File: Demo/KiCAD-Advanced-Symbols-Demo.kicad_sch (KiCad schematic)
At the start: 15 parts

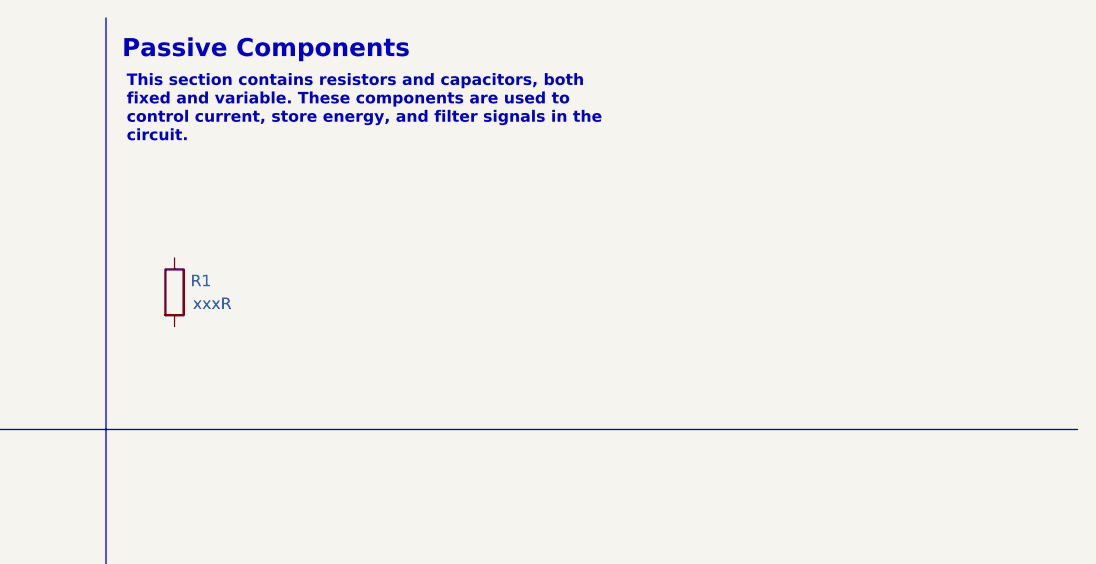
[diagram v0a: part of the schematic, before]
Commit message: Add general and specialized diode symbols, fixed capacitor, and potentiometer
Added new components to library: general diode symbols (Diode_General, Diode_General_45), fixed capacitor (Capacitor_Fixed), bridge rectifier (Diode_Bridge_4Way), specialized diodes (Diode_Schottky, Diode_Zener, Diode_LED, Diode_Photodiode), and variable resistor (Resistor_Potentiometer).
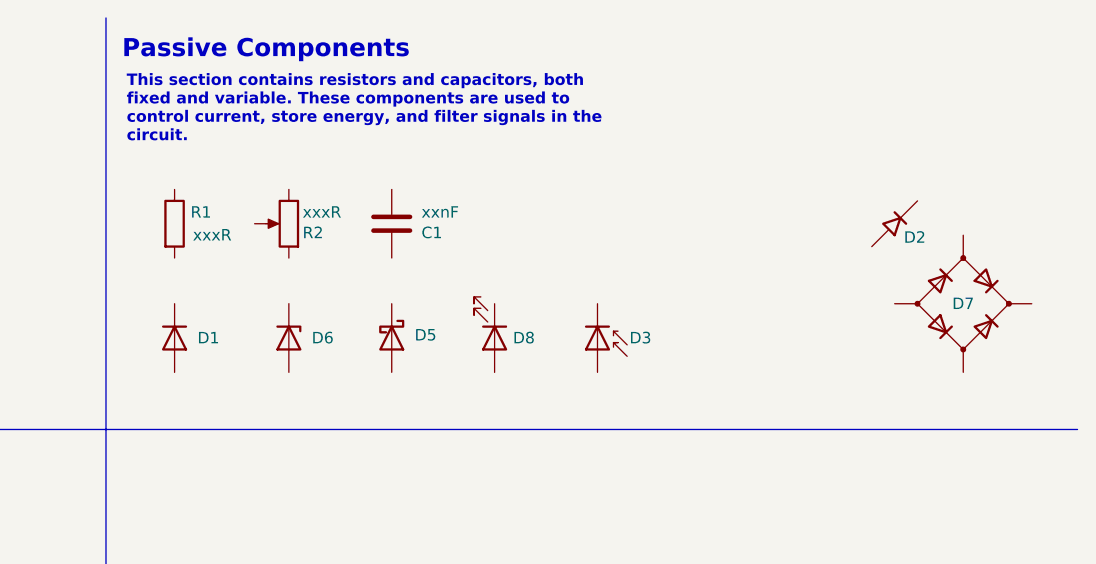
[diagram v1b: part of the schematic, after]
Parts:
- added C1: xxnF, symbol KiCAD-Advanced-Symbols:Capacitor_Fixed
- added D1: Typ, symbol KiCAD-Advanced-Symbols:Diode_General
- added D2: Typ, symbol KiCAD-Advanced-Symbols:Diode_General_45
- added D3: ~, symbol KiCAD-Advanced-Symbols:Diode_Photodiode
- added D5: Typ, symbol KiCAD-Advanced-Symbols:Diode_Schottky
- added D6: Typ, symbol KiCAD-Advanced-Symbols:Diode_Zener
- added D7: ~, symbol KiCAD-Advanced-Symbols:Diode_Bridge_4Way
- added D8: ~, symbol KiCAD-Advanced-Symbols:Diode_LED
- added R2: xxxR, symbol KiCAD-Advanced-Symbols:Resistor_Potentiometer
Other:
- moved on the sheet: R1
